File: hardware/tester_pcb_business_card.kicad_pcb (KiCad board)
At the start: 2 copper layers, 83.8 x 53.3 mm, 46 parts, among them J1 SWIO, SW1 PWR, SW2 A, SW3 B, SW4 C, SW5 D, SW6 RST, U1 CH32V003FxUx

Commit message: Update LED resistor values after tuning
LEDs were way too bright with chosen resistor values. Tuned so all LEDs are of a similar brightness and to reduce current draw.
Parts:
- R1, R11, R13, R15, R17, R19, R2, R3, R4, R5: value 220 -> 470
- R12, R14, R16, R18, R20: value 100 -> 3.3k

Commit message: Fix test case LEDs rows and cols
I had them labelled the wrong way round. Didn't affect anything but it was confusing when referring to schematic when writing code for the test case LEDs.
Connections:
- net /COL_G renamed /ROW_G
- net /COL_R renamed /ROW_R
- net /ROW_A renamed /COL_A
- net /ROW_B renamed /COL_B
- net /ROW_C renamed /COL_C
- net /ROW_D renamed /COL_D
- net /ROW_E renamed /COL_E

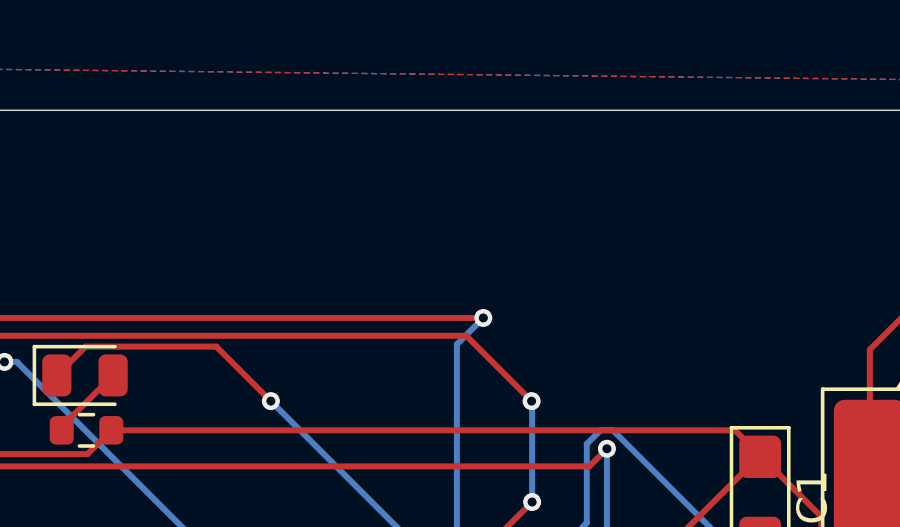
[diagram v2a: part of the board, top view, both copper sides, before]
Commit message: PCBs for Ministry of Testing TestBash Brighton 2025
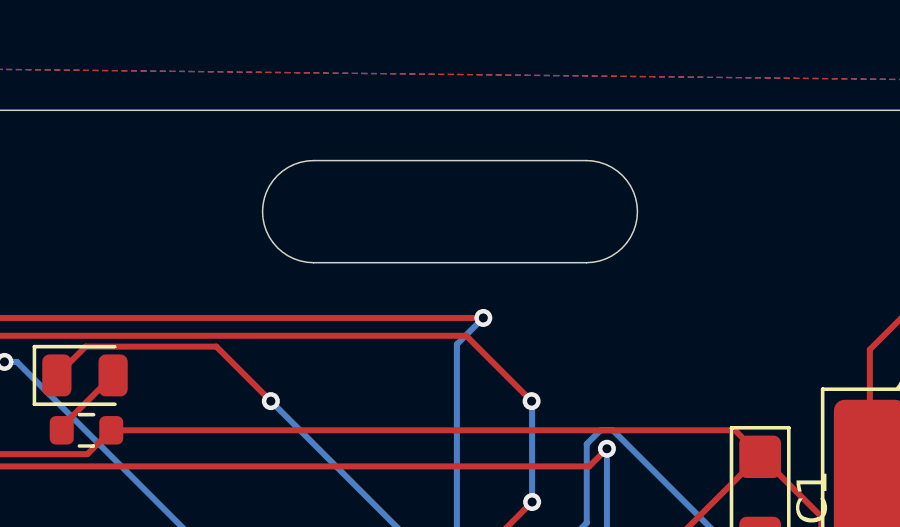
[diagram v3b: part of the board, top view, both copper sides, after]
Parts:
- added G***: LOGO, custom:mot_bug, B.Cu at (62.6, 78.7)
- added G***: LOGO, custom:testbash_2025_16mm, B.Cu at (127.7, 78.8)
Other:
- outline, holes or cut-outs redrawn
- board text added: "LinkedIn ^"
- board text added: "Ministry of Testing TestBash Brighton 2025 Edition"
- board text added: "Not affiliated with Ministry of Testing. Just a fan-made artifact celebrating Brighton TestBash 2025."
- board text added: "https://www.ministryoftesting.com/"
- board text added: "https://www.ministryoftesting.com/p/markjb"
